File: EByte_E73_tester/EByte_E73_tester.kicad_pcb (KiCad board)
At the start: 2 copper layers, 77.5 x 49.5 mm, 42 parts, among them J1 Serial Connector, J2 Serial Connector, J3 Conn_01x04, J4 Conn_01x06, J5 Conn_01x04, J6 Conn_01x02, Q1 Q_PMOS_GSD, SW1 RESET, SW2 RESET, SW3 RESET, SW4 RESET, SW5 RESET, SW6 SW_SPDT, U1 E73-2G4M04S, U2 ProMicro, U3 AP2112K-3.3, U4 TP4056

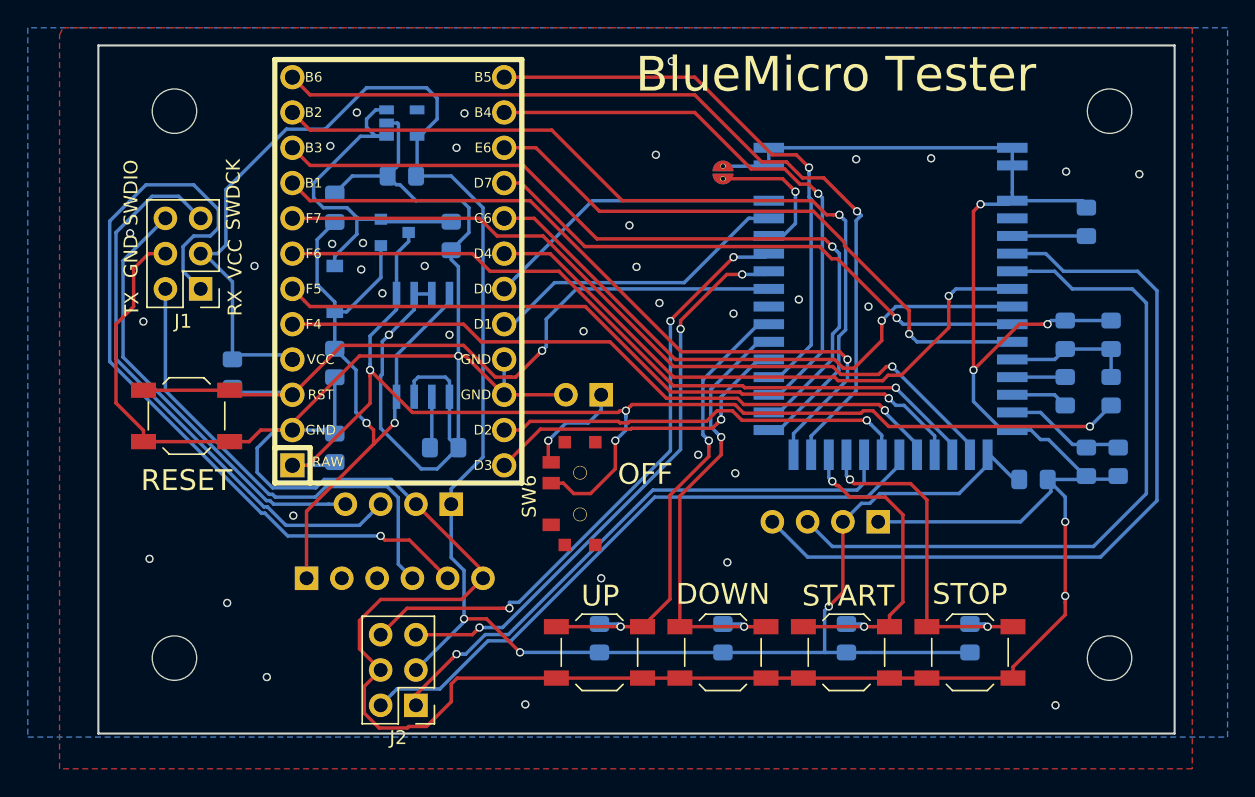
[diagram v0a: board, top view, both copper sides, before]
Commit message: adding BlueNano V2.0 Schematic
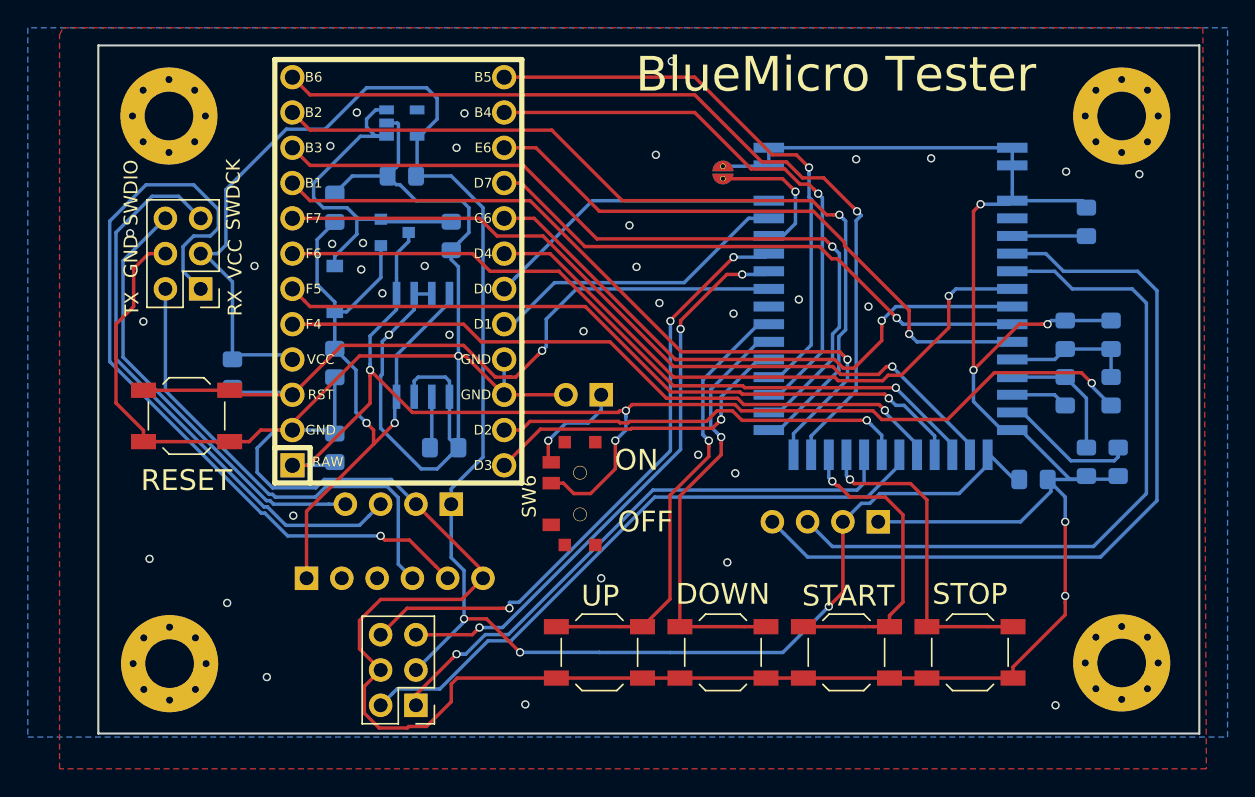
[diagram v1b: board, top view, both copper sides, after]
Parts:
- removed R6, R7, R8, R9: 10k, Resistor_SMD:R_0805_2012Metric_Pad1.15x1.40mm_HandSolder
- removed REF1, REF2, REF3, REF4: MountingHole_3.2mm_M3_DIN965, MountingHole:MountingHole_3.2mm_M3_DIN965
- added J10: Conn_01x01, MountingHole:MountingHole_3.5mm_Pad_Via, F.Cu at (134.6, 87.6)
- added J7: Conn_01x01, MountingHole:MountingHole_3.5mm_Pad_Via, F.Cu at (134.6, 127.0)
- added J8: Conn_01x01, MountingHole:MountingHole_3.5mm_Pad_Via, F.Cu at (66.0, 87.6)
- added J9: Conn_01x01, MountingHole:MountingHole_3.5mm_Pad_Via, F.Cu at (66.1, 127.0)
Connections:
- C2 pad 1: Net-(C1-Pad1) -> Net-(C2-Pad1)
- J4 pad 2: Net-(J4-Pad2) -> (no net)
- J4 pad 3: Net-(J4-Pad3) -> (no net)
- L1 pad 1: Net-(L1-Pad1) -> Net-(C1-Pad1)
- SW6 pad 1: Net-(SW6-Pad1) -> (no net)
- U1 pad 12: Net-(L1-Pad1) -> Net-(C1-Pad1)
- U1 pad 14: Net-(C1-Pad1) -> Net-(C2-Pad1)
- U1 pad 3: Net-(U1-Pad3) -> (no net)
- U1 pad 35: DFU -> (no net)
- U3 pad 4: Net-(U3-Pad4) -> (no net)
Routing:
- net VCC: track 148.6 -> 136.4 mm
- net Net-(C2-Pad1): track 0.00 -> 9.85 mm
- net Net-(L1-Pad1): track 3.81 -> 0.00 mm
- net /P0.19: track 34.1 -> 32.5 mm, vias 2 -> 1
- net /P0.18: track 32.0 -> 30.4 mm, vias 2 -> 1
- net /VBatt: track 90.5 -> 92.0 mm
- net /P0.09: track 24.7 -> 23.4 mm, vias 2 -> 1
- net /P0.10: track 24.1 -> 22.8 mm, vias 2 -> 1
- net Net-(C1-Pad1): track 8.58 -> 9.52 mm
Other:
- board size 77.5 x 49.5 mm -> 79.2 x 49.5 mm
- board text added: "ON"
